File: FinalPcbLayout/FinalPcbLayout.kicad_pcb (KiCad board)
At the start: 4 copper layers, 100.9 x 47.2 mm, 64 parts, among them J1 Conn_02x05_Odd_Even, J2 Conn_01x04_Pin, J3 Barrel_Jack, J4 Conn_01x11_Pin, J5 USB_C_Receptacle, J6 Conn_01x02_Pin, J8 Micro_SD_Card, Q1 NMOS, SW1 SW_Push, U1 ESP32-WROOM-32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

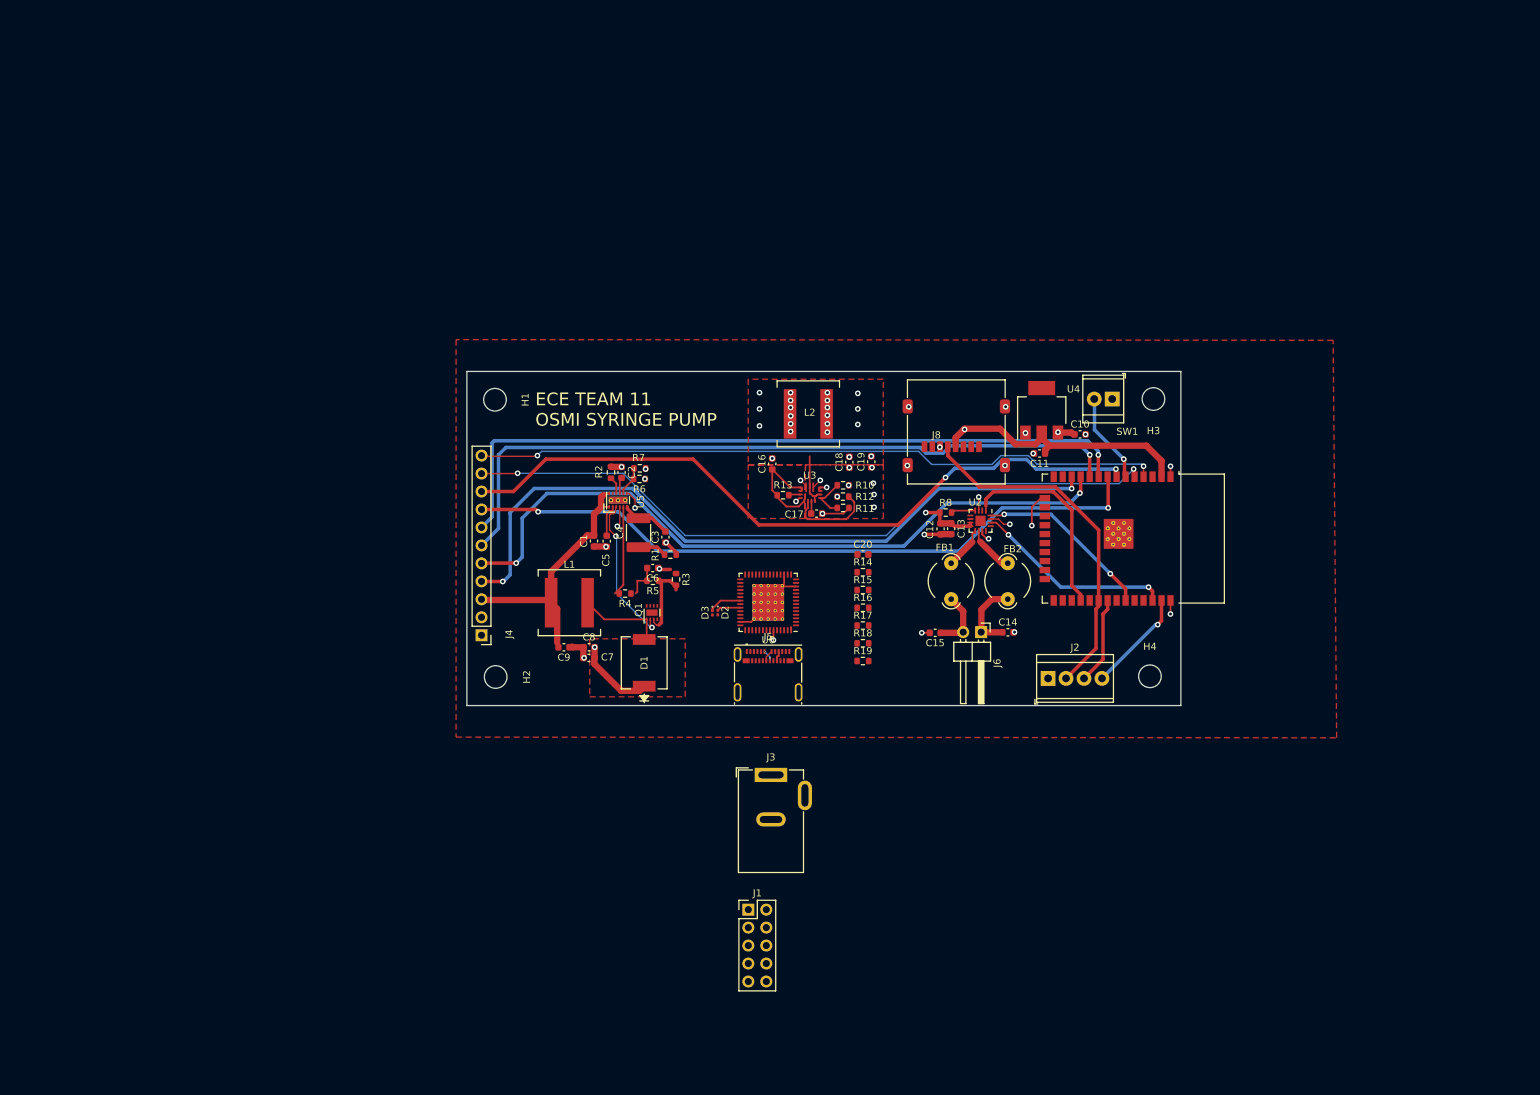
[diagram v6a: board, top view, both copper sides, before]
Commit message: No ERC Errors
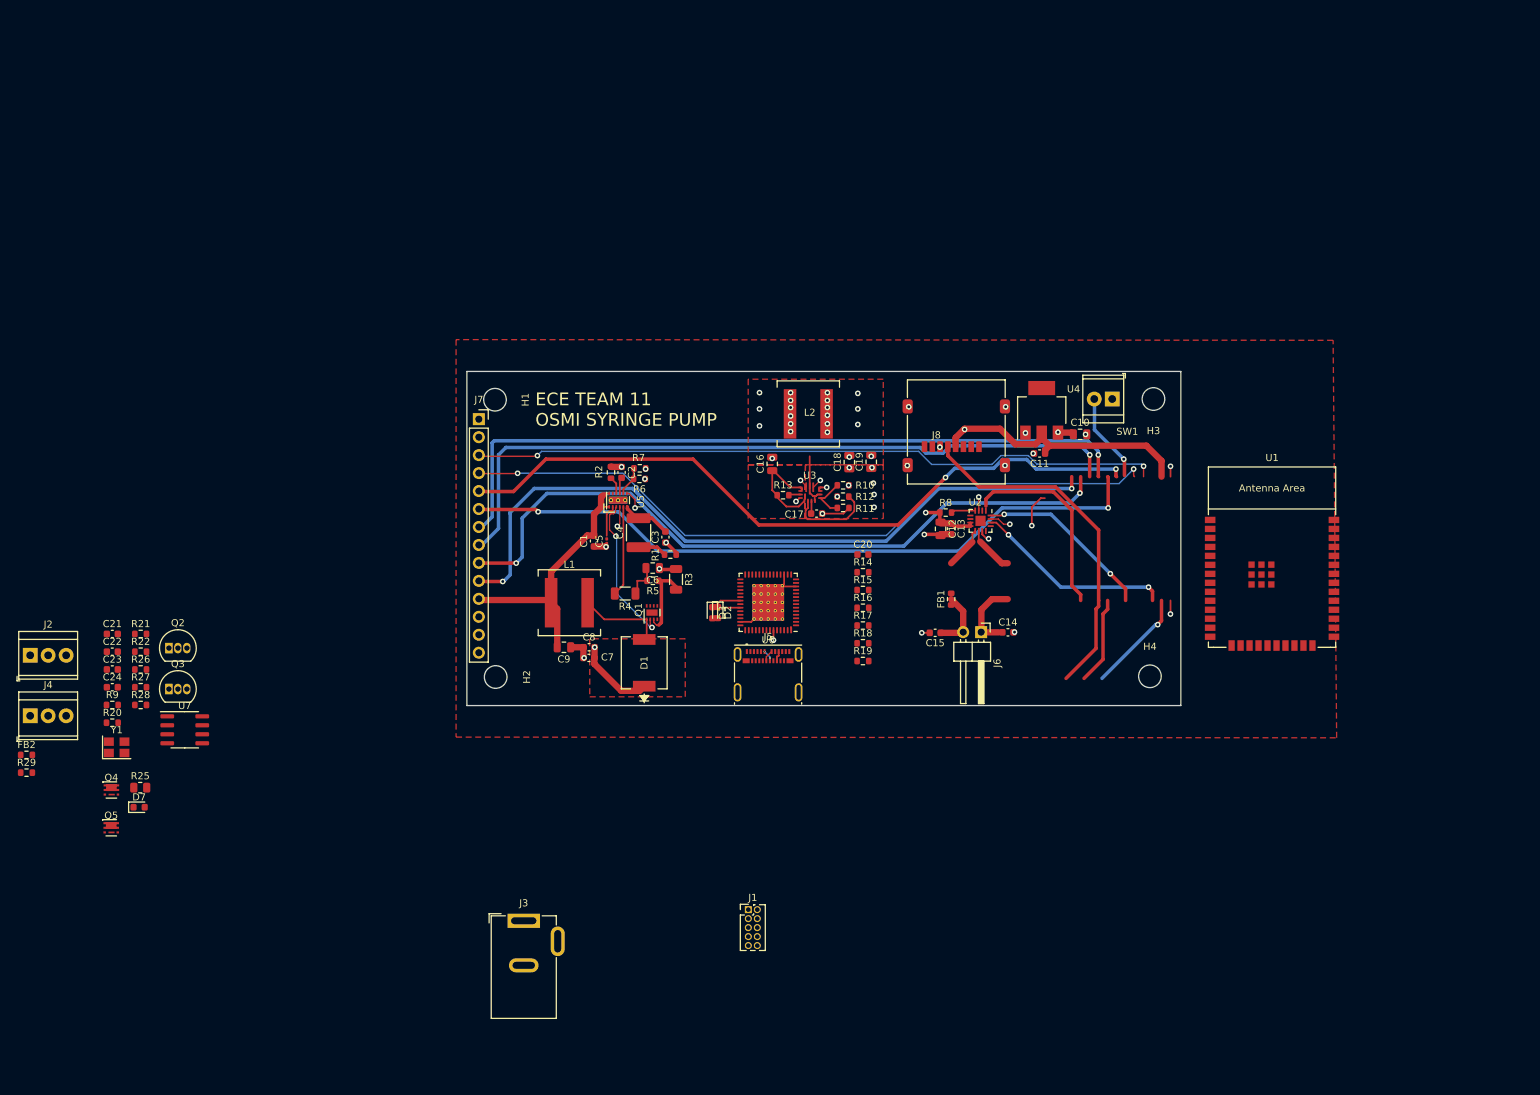
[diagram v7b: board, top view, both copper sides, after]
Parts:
- added C21: 18pf, Capacitor_SMD:C_0603_1608Metric, F.Cu at (32.0, 116.2)
- added C22: 18pf, Capacitor_SMD:C_0603_1608Metric, F.Cu at (32.0, 118.7)
- added C23: 33nF, Capacitor_SMD:C_0603_1608Metric, F.Cu at (32.0, 121.2)
- added C24: .1u, Capacitor_SMD:C_0603_1608Metric, F.Cu at (32.0, 123.7)
- added D7: RED, LED_SMD:LED_0603_1608Metric, F.Cu at (35.8, 140.7)
- added J7: Display Socket, Connector_PinSocket_2.54mm:PinSocket_1x14_P2.54mm_Vertical, F.Cu at (83.8, 85.9)
- added Q2: S8050, Package_TO_SOT_THT:TO-92_Inline, F.Cu at (40.0, 118.2)
- added Q3: S8050, Package_TO_SOT_THT:TO-92_Inline, F.Cu at (40.0, 124.0)
- added Q4: PMOS, Package_TO_SOT_SMD:Vishay_PowerPAK_SC70-6L_Single, F.Cu at (31.9, 138.3)
- added Q5: PMOS, Package_TO_SOT_SMD:Vishay_PowerPAK_SC70-6L_Single, F.Cu at (31.8, 143.6)
- added R20: 100k 1%, Resistor_SMD:R_0603_1608Metric, F.Cu at (32.0, 128.8)
- added R21: 15k 1%, Resistor_SMD:R_0603_1608Metric, F.Cu at (36.0, 116.2)
- added R22: 2k, Resistor_SMD:R_0603_1608Metric, F.Cu at (36.0, 118.7)
- added R25: 100, Resistor_SMD:R_0805_2012Metric, F.Cu at (35.9, 137.9)
- added R26: 10k, Resistor_SMD:R_0603_1608Metric, F.Cu at (36.0, 121.2)
- added R27: 10k, Resistor_SMD:R_0603_1608Metric, F.Cu at (36.0, 123.7)
- added R28: 10k, Resistor_SMD:R_0603_1608Metric, F.Cu at (36.0, 126.3)
- added R29: 10k, Resistor_SMD:R_0603_1608Metric, F.Cu at (19.9, 135.8)
- added R9: 12k 1%, Resistor_SMD:R_0603_1608Metric, F.Cu at (32.0, 126.3)
- added U7: 93LCxxB, Package_SO:SOIC-8_3.9x4.9mm_P1.27mm, F.Cu at (42.2, 129.8)
- added Y1: 12Mhz, Crystal:Crystal_SMD_SeikoEpson_FA238-4Pin_3.2x2.5mm, F.Cu at (32.6, 132.2)
- C10, C12, C16, C18, C19, C6, C9: footprint Capacitor_SMD:C_0603_1608Metric -> Capacitor_SMD:C_0805_2012Metric
- C5: footprint Capacitor_SMD:C_0603_1608Metric -> Capacitor_SMD:C_0201_0603Metric
- D2: value LED -> BLUE; footprint LED_SMD:LED_0201_0603Metric -> LED_SMD:LED_0603_1608Metric
- D3: value LED -> RED; footprint LED_SMD:LED_0201_0603Metric -> LED_SMD:LED_0603_1608Metric
- FB1, FB2: footprint Ferrite_THT:LairdTech_28C0236-0JW-10 -> Resistor_SMD:R_0603_1608Metric
- J1: footprint Connector_PinHeader_2.54mm:PinHeader_2x05_P2.54mm_Vertical -> Connector_PinHeader_1.27mm:PinHeader_2x05_P1.27mm_Vertical
- J2: value Conn_01x04_Pin -> SPI; footprint TerminalBlock_TE-Connectivity:TerminalBlock_TE_282834-4_1x04_P2.54mm_Horizontal -> TerminalBlock_TE-Connectivity:TerminalBlock_TE_282834-3_1x03_P2.54mm_Horizontal
- J4: value Conn_01x11_Pin -> C1; footprint Connector_PinHeader_2.54mm:PinHeader_1x11_P2.54mm_Vertical -> TerminalBlock_TE-Connectivity:TerminalBlock_TE_282834-3_1x03_P2.54mm_Horizontal
- R18: value ??? -> 25
- R19: value ??? -> 65
- R3, R4: footprint Resistor_SMD:R_0603_1608Metric -> Resistor_SMD:R_1206_3216Metric
- U1: value ESP32-WROOM-32 -> ESP32-WROOM-E; footprint RF_Module:ESP32-WROOM-32 -> PCM_Espressif:ESP32-WROOM-32E
- moved J2 143.9 mm to (20.4, 119.2)
- moved FB2 140.5 mm to (19.9, 133.3), turned to 0 degrees
- moved J4 64.8 mm to (20.4, 127.8), turned to 0 degrees
- moved J3 40.6 mm to (90.2, 156.8)
- moved U1 23.0 mm to (196.0, 107.1), turned to 0 degrees
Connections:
- net Net-(J5-VBUS-PadA4) renamed /Power/USB_Vin
- J2 pad 1: GND -> /COPI
- J2 pad 2: /SCLK -> /CIPO
- J2 pad 3: /CIPO -> /SCLK
- J4 pad 1: GND -> /C1_PWM
- J4 pad 2: +3.3V -> /C1_CS
- J4 pad 3: +5V -> /C1_Limit
- J8 pad 2: unconnected-(J8-DAT3/CD-Pad2) -> /SD_CS
- J8 pad 3: unconnected-(J8-CMD-Pad3) -> /COPI
- J8 pad 7: unconnected-(J8-DAT0-Pad7) -> /CIPO
- R16 pad 2: /usb/RXD -> /TXD
- R17 pad 2: /usb/TXD -> /RXD
- U1 pad 10: /IO25 -> /C1_Limit
- U1 pad 11: /IO26 -> /C1_PWM
- U1 pad 12: /IO27 -> /C1_CS
- U1 pad 14: /JTAG_TCK -> /JTAG_TDI
- U1 pad 16: /JTAG_TDI -> /JTAG_TCK
- U1 pad 17: unconnected-(U1-SHD/SD2-Pad17) -> (no net)
- U1 pad 18: unconnected-(U1-SWP/SD3-Pad18) -> (no net)
- U1 pad 19: unconnected-(U1-SCS/CMD-Pad19) -> (no net)
- U1 pad 20: unconnected-(U1-SCK/CLK-Pad20) -> (no net)
- U1 pad 21: unconnected-(U1-SDO/SD0-Pad21) -> (no net)
- U1 pad 22: unconnected-(U1-SDI/SD1-Pad22) -> (no net)
- U1 pad 25: unconnected-(U1-IO0-Pad25) -> /ESP_IO0_B
- U1 pad 3: unconnected-(U1-EN-Pad3) -> /ESP_EN
- U1 pad 32: unconnected-(U1-NC-Pad32) -> (no net)
- U1 pad 34: unconnected-(U1-RXD0/IO3-Pad34) -> /TXD
- U1 pad 35: unconnected-(U1-TXD0/IO1-Pad35) -> /RXD
- U1 pad 4: /Sense_VP -> unconnected-(U1-SENSOR_VP/GPIO36/ADC1_CH0-Pad4)
- U1 pad 5: /Sense_VN -> unconnected-(U1-SENSOR_VN/GPIO39/ADC1_CH3-Pad5)
- U1 pad 7: /IO35 -> /SD_CS
- U6 pad 48: unconnected-(U6-DM-Pad48) -> /usb/D-
- U6 pad 49: unconnected-(U6-DP-Pad49) -> /usb/D+
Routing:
- net /SCLK: track 49.8 -> 254.6 mm, vias 0 -> 3
- net /IO33: track 102.8 -> 0.00 mm, vias 1 -> 0
- net /IO25: track 102.2 -> 0.00 mm, vias 1 -> 0
- net +3.3V: track 130.2 -> 232.4 mm, vias 1 -> 2
- net /IO27: track 102.0 -> 0.00 mm, vias 2 -> 0
- net unconnected-(J7-Pin_9-Pad9): track 0.00 -> 101.1 mm, vias 0 -> 2
- net /IO26: track 101.1 -> 0.00 mm, vias 2 -> 0
- net /IO35: track 101.0 -> 0.00 mm, vias 2 -> 0
- net /Display_DC: track 0.00 -> 101.0 mm, vias 0 -> 2
- net /Sense_VN: track 100.9 -> 0.00 mm, vias 2 -> 0
- net /Display_RST: track 0.00 -> 100.9 mm, vias 0 -> 2
- net /COPI: track 14.7 -> 112.7 mm, vias 1 -> 3
- net /IO32: track 98.0 -> 0.00 mm, vias 2 -> 0
- net /Sense_VP: track 97.3 -> 0.00 mm, vias 2 -> 0
- net /Display_CS: track 0.00 -> 97.3 mm, vias 0 -> 2
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
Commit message: All changes imported to PCB
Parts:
- moved J4 140.4 mm to (160.8, 125.0)
- moved J2 126.1 mm to (145.5, 134.4)
- moved U1 21.8 mm to (174.6, 102.9), turned to -90 degrees
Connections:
- Q4 pad 3: /Power/V_in -> GND
- Q4 pad 4: (no net) -> /Power/V_in
- Q5 pad 3: /Power/V_in -> GND
- Q5 pad 4: (no net) -> /Power/V_in
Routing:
- net GND: track 53.2 -> 48.7 mm, vias 36 -> 35
